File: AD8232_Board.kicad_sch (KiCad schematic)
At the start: 0 parts

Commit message: Library and Schematic Update
- Updated the AD8232 Symbol to include 21 pins with the 21st auto connected to ground.
- Completed the schematic for the board and attached footprints to them.
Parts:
- added C1: 1nF, Capacitor_SMD:C_0603_1608Metric, symbol Device:C
- added C2: 10nF, Capacitor_SMD:C_0603_1608Metric, symbol Device:C
- added C3: 1.5nF, Capacitor_SMD:C_0603_1608Metric, symbol Device:C
- added C4, C5: 0.1uF, Capacitor_SMD:C_0603_1608Metric, symbol Device:C
- added C6, C7: 0.33uF, Capacitor_SMD:C_0603_1608Metric, symbol Device:C
- added D1: LED, LED_SMD:LED_0603_1608Metric, symbol Device:LED
- added J1, J2: Conn_01x05_Pin, Connector_PinHeader_2.54mm:PinHeader_1x05_P2.54mm_Vertical, symbol Connector:Conn_01x05_Pin
- added R1: 180K, Resistor_SMD:R_0805_2012Metric, symbol Device:R
- added R10, R11, R12, R13, R14, R3, R4: 10M, Resistor_SMD:R_0603_1608Metric, symbol Device:R
- added R15: 470, Resistor_SMD:R_0805_2012Metric, symbol Device:R
- added R2: 180K, Resistor_SMD:R_0815_2038Metric, symbol Device:R
- added R5: 360K, Resistor_SMD:R_1206_3216Metric, symbol Device:R
- added R6, R8, R9: 1M, Resistor_SMD:R_0805_2012Metric, symbol Device:R
- added R7: 100K, Resistor_SMD:R_0603_1608Metric, symbol Device:R
- added U1: AD8232, Package_DFN_QFN:QFN-20-1EP_4x4mm_P0.5mm_EP2.6x2.6mm, symbol AD8232_Library:AD8232
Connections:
- new net: R12.2, R13.2, R14.2
- new net: C5.1, R10.2, R11.2, U1.18 (REFIN)
- new net: C1.1, U1.4 (RLDFB)
- new net: C1.2, R5.2, U1.5 (RLD)
- new net: R2.2, U1.3 (-IN)
- new net: R9.1, U1.7 (OPAMP+)
- new net: C2.1, R8.1, R9.2
- new net: R6.1, R7.2, U1.9 (OPAMP-)
- new net: R1.2, U1.2 (+IN)
- new net: C6.1, U1.1 (HPDRIVE)
- new net: C6.2, R12.1, U1.20 (HPSENSE)
- new net: D1.2 (A), R15.2
- new net +3.3V: C4.1, J2.1 (Pin_1), R10.1, R3.2, R4.2, U1.15 (FR), U1.17 (+Vs)
- new net GND: C4.2, C5.2, D1.1 (K), J2.2 (Pin_2), R11.1, U1.14 (AC/DC), U1.16 (GND), U1.21 (GND)
- new net IAOUT: C3.1, R13.1, R8.2, U1.19 (IAOUT)
- new net LA: J1.1 (Pin_1), R1.1, R3.1
- new net LO+: J2.3 (Pin_3), U1.12 (LO+)
- new net LO-: J2.4 (Pin_4), U1.11 (LO-)
- new net RA: J1.2 (Pin_2), R2.1, R4.1
- new net REFOUT: C2.2, C7.2, R7.1, U1.8 (REFOUT)
- new net RL: J1.3 (Pin_3), R5.1
- new net SDN: J2.5 (Pin_5), U1.13 (SDN)
- new net SIGNAL OUTPUT: C3.2, J1.4 (Pin_4), R15.1, R6.2, U1.10 (OUT)
- new net SW: C7.1, R14.1, U1.6 (SW)
- no-connect marks 0 -> 1

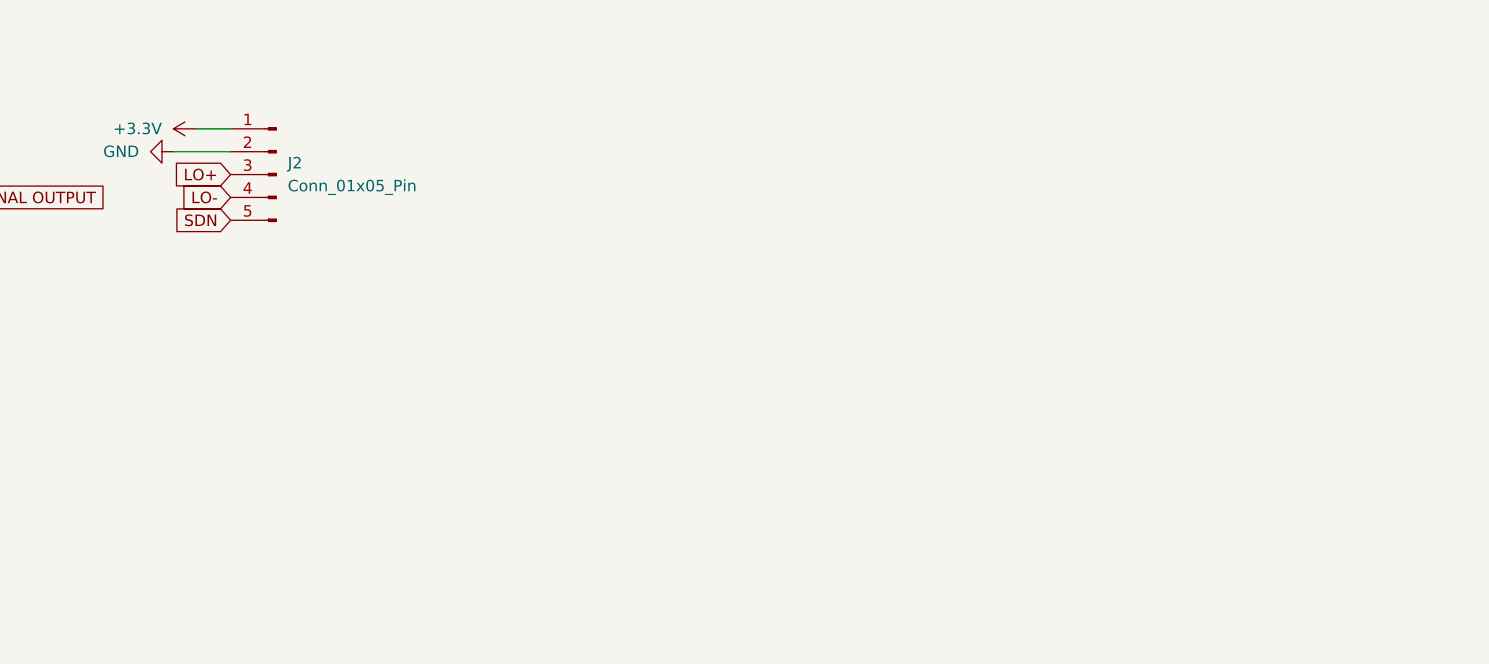
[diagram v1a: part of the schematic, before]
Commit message: PCB designed and Gerber files generated
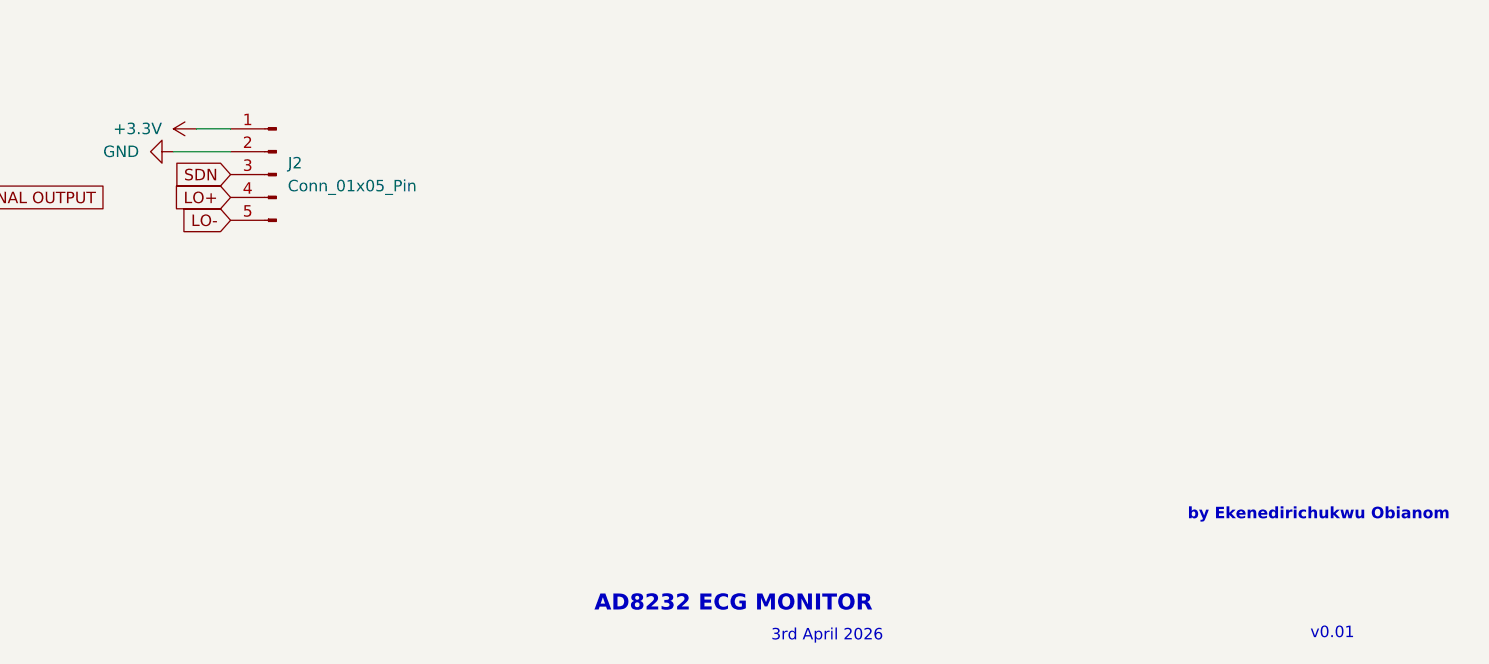
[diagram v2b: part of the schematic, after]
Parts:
- R2: footprint Resistor_SMD:R_0815_2038Metric -> Resistor_SMD:R_0805_2012Metric
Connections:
- net LO+: now also J2.4 (Pin_4); no longer J2.3 (Pin_3)
- net LO-: now also J2.5 (Pin_5); no longer J2.4 (Pin_4)
- net SDN: now also J2.3 (Pin_3); no longer J2.5 (Pin_5)
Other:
- note added: "3rd April 2026"
- note added: "AD8232 ECG MONITOR"
- note added: "by Ekenedirichukwu Obianom"
- note added: "v0.01"
